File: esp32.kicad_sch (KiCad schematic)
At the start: 46 parts, among them J5 Conn_01x05, SW2 BOOT, U6 ESP32-S3R8, U7 W25Q128JVSIQ, Y1 40MHz

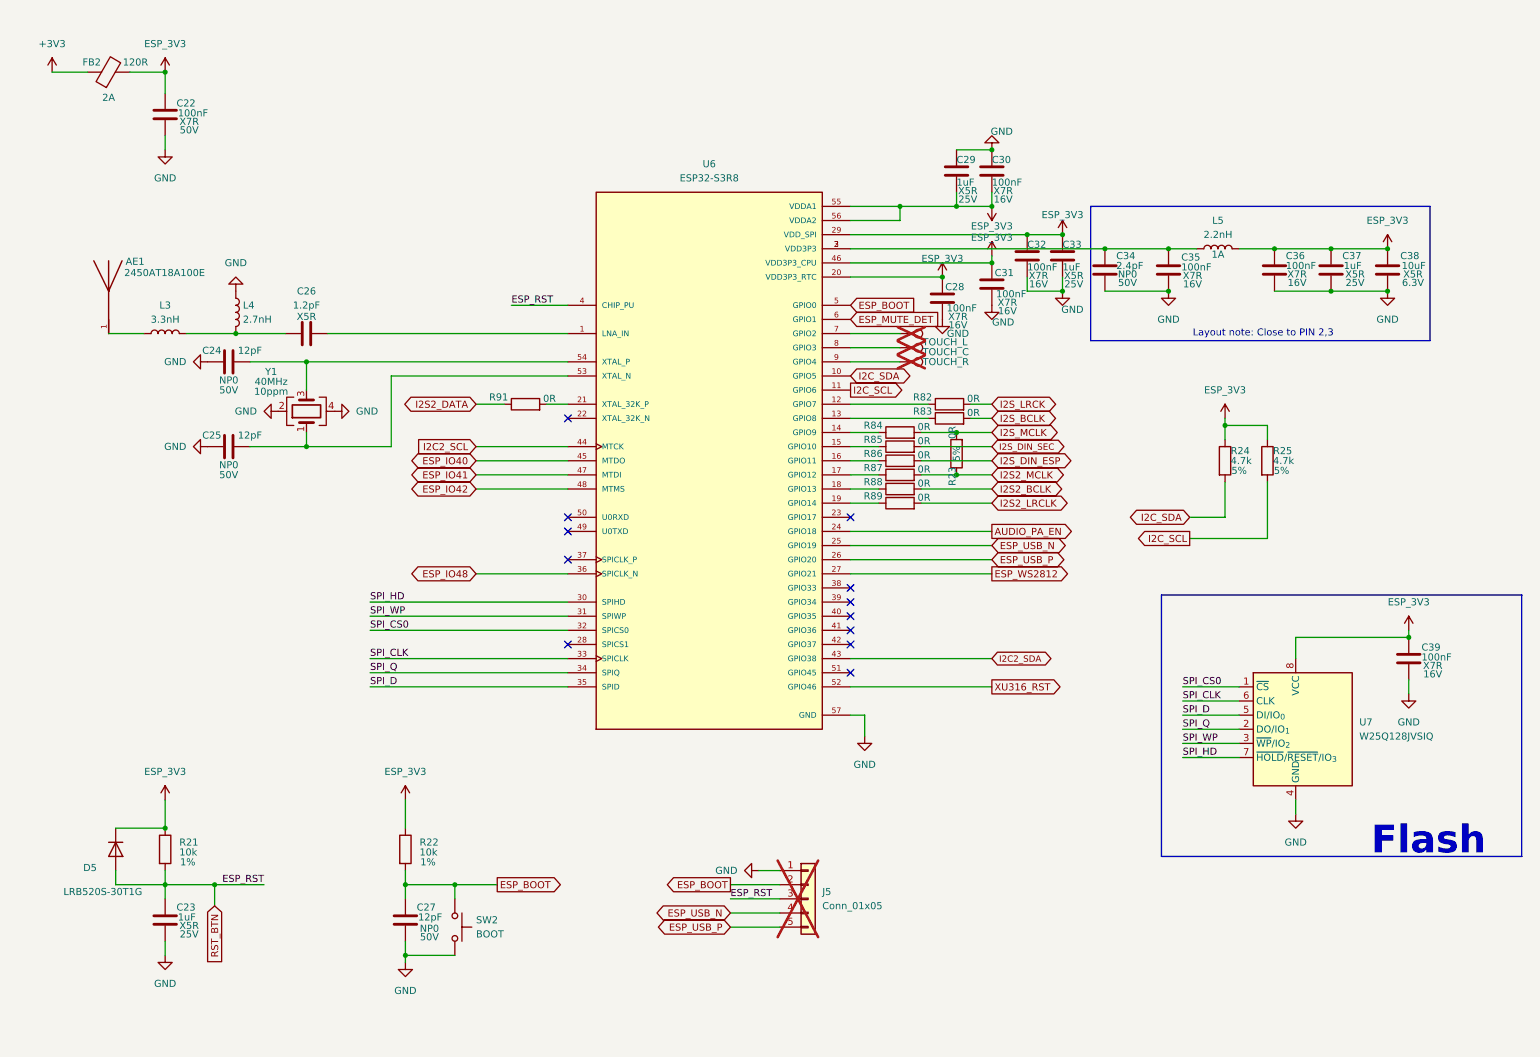
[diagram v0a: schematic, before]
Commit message: v2 hardware revision
MPR121 touch controller added to replace esp32-s3 integrated touch pins
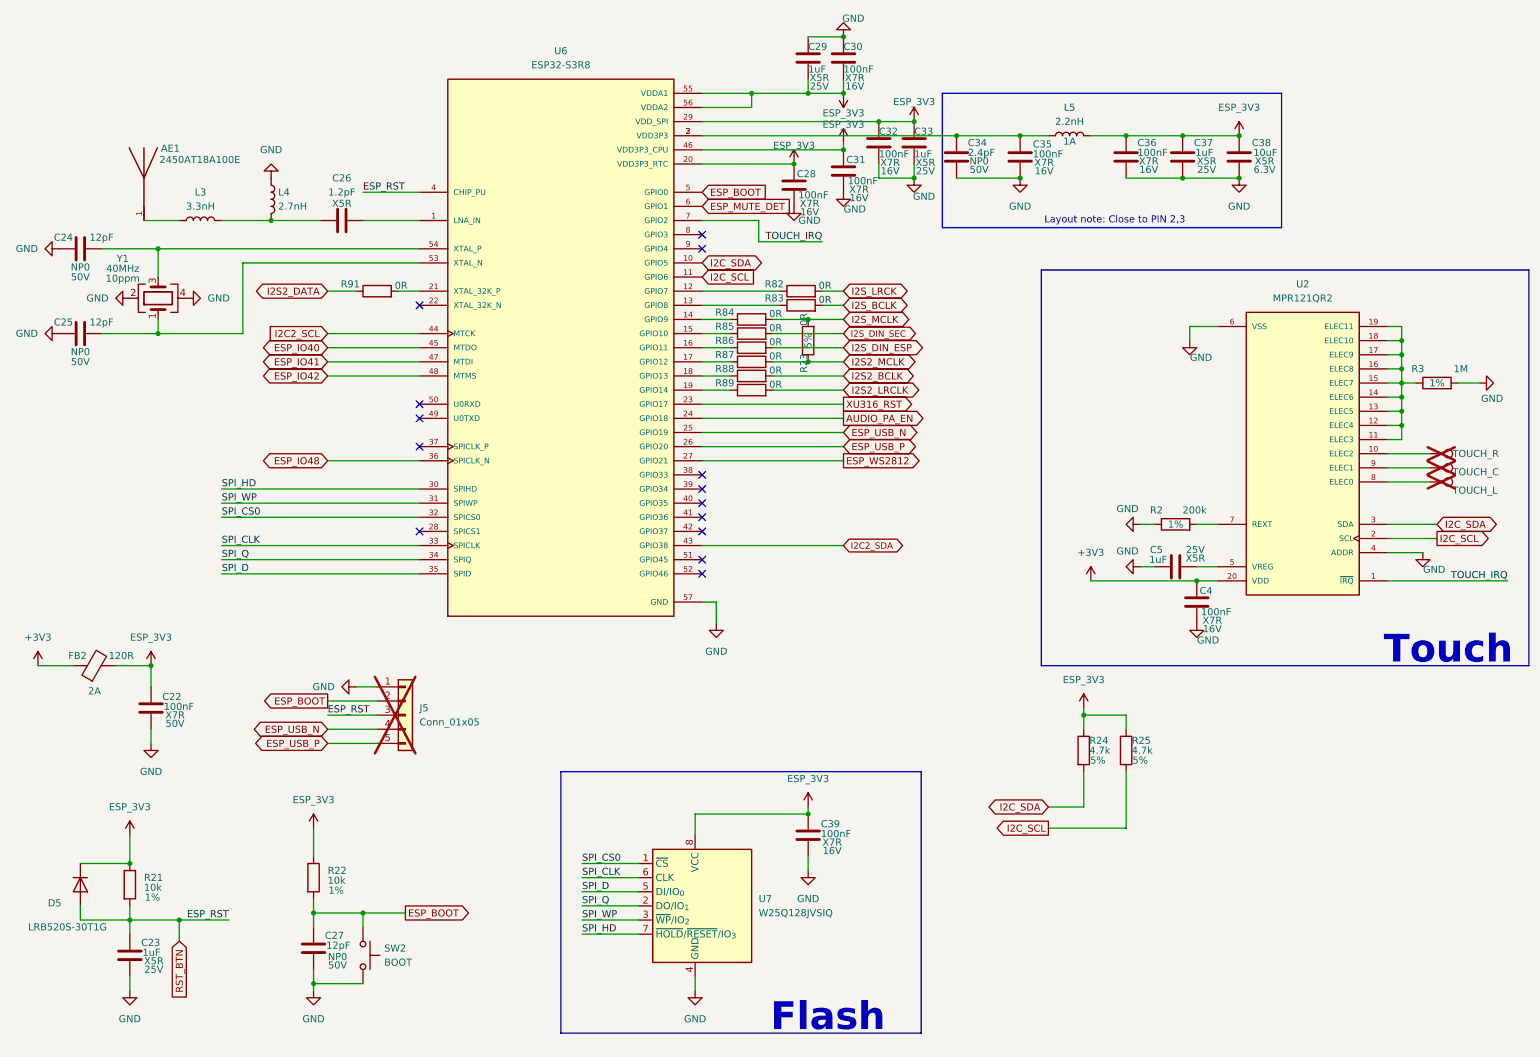
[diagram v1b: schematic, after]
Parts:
- added C4: 100nF, Capacitor_SMD:C_0402_1005Metric, symbol Device:C
- added C5: 1uF, Capacitor_SMD:C_0402_1005Metric, symbol Device:C
- added R2: 200k, Resistor_SMD:R_0402_1005Metric, symbol Device:R
- added R3: 1M, Resistor_SMD:R_0402_1005Metric, symbol Device:R
- added U2: MPR121QR2, Onju:MPR121QR2, symbol New_Library:MPR121QR2
- AE1: Manufacturer Part Number 2450AT18A100E -> (none); PARTREV 1.3 -> (none)
- C23: Supplier Part C52923 -> (none)
- C27: Supplier Part C1547 -> (none)
- D5: Supplier Part C83680 -> (none)
- FB2: Part number BLM18PG121SN1D -> (none)
- R21, R22: Supplier Part C25744 -> (none)
- R82, R83, R84, R85, R86, R87, R88, R89: Function (none) -> ESP32
- R91: Function (none) -> XMOS
- SW2: Supplier Part C221897 -> (none)
- U6: Availability In Stock -> (none); Check_prices https://www.snapeda.com/parts/ESP32-S3R8/Espressif+Systems/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 -> (none)
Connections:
- net +3V3: now also C4.1, U2.20 (VDD)
- net GND: now also C4.2, C5.1, R2.1, R3.2, U2.4 (ADDR), U2.6 (VSS)
- net I2C_SCL: now also U2.2 (SCL)
- net I2C_SDA: now also U2.3 (SDA)
- net XU316_RST: now also U6.23 (GPIO17); no longer U6.52 (GPIO46)
- net at TP8.1: now also U2.10 (ELEC2); no longer U6.9 (GPIO4)
- net at TP6.1: now also U2.8 (ELEC0); no longer U6.7 (GPIO2)
- net at TP7.1: now also U2.9 (ELEC1); no longer U6.8 (GPIO3)
- new net: R3.1, U2.11 (ELEC3), U2.12 (ELEC4), U2.13 (ELEC5), U2.14 (ELEC6), U2.15 (ELEC7), U2.16 (ELEC8), U2.17 (ELEC9), U2.18 (ELEC10), U2.19 (ELEC11)
- new net: C5.2, U2.5 (VREG)
- new net: R2.2, U2.7 (REXT)
- new net TOUCH_IRQ: U2.1 (~{IRQ}), U6.7 (GPIO2)
- no-connect marks 12 -> 14
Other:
- note added: "Touch"
- moved on the sheet: AE1, C22, C23, C24, C25, C26, C27, C28, C29, C30, C31, C32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
